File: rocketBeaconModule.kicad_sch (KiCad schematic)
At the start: 36 parts, among them J1 TYPE-C-31-M-12, J2 Jumper Select, J3 Main Bus, U1 STM32F401CCU6, U2 AMS1117-3.3, Y1 16MHz

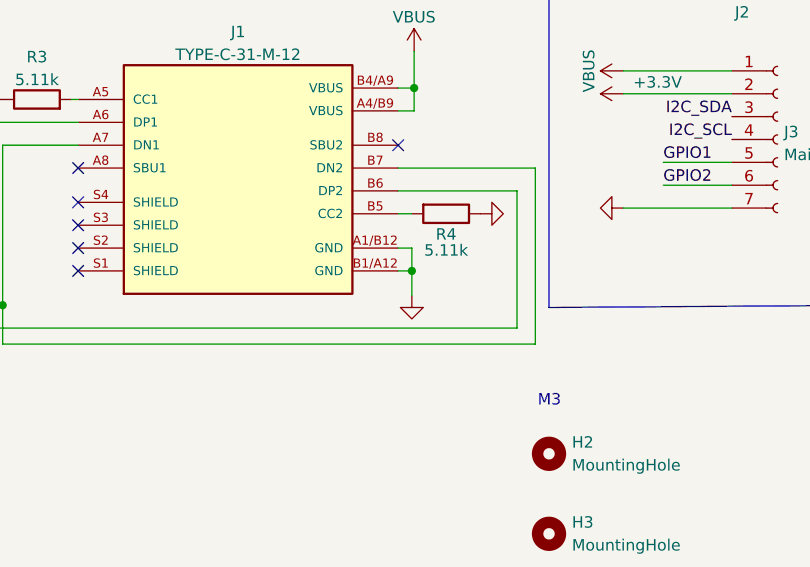
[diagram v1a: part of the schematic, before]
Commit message: removed old footprints and replaced with new ones
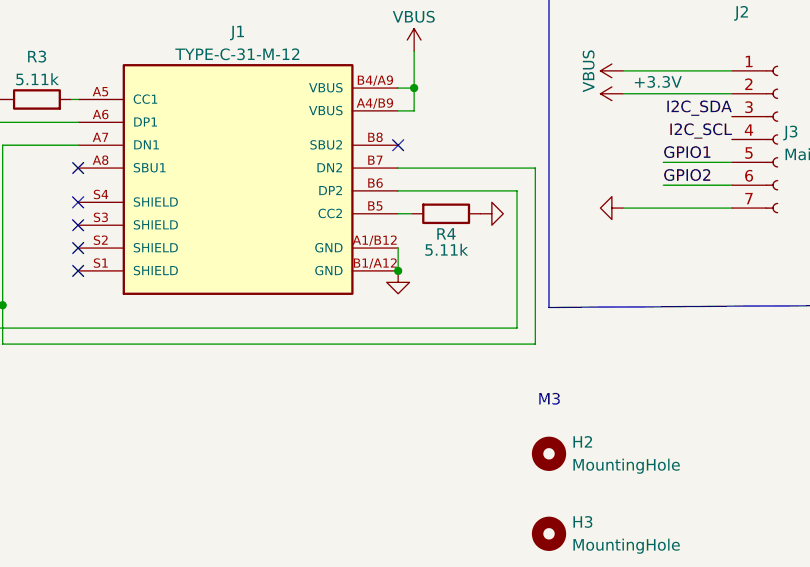
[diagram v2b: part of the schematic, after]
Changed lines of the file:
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@@
   (junction (at 88.9 24.13) (diameter 0) (color 0 0 0 0)
   )
-  (junction (at 233.68 102.87) (diameter 0) (color 0 0 0 0)
-  )
   (junction (at 135.89 124.46) (diameter 0) (color 0 0 0 0)
   )
@@
   )
   (junction (at 129.54 36.83) (diameter 0) (color 0 0 0 0)
+  )
+  (junction (at 232.156 102.87) (diameter 0) (color 0 0 0 0)
   )
   (junction (at 88.9 36.83) (diameter 0) (color 0 0 0 0)
@@
   (no_connect (at 118.11 76.2))
   (no_connect (at 118.11 101.6))
-  (wire (pts (xy 233.68 100.33) (xy 233.68 102.87))
-    (stroke (width 0) (type default) (color 0 0 0 0))
-  )
   (wire (pts (xy 135.89 121.92) (xy 135.89 124.46))
     (stroke (width 0) (type default) (color 0 0 0 0))
@@
     (stroke (width 0) (type default) (color 0 0 0 0))
   )
-  (wire (pts (xy 233.68 102.87) (xy 233.68 105.664))
-    (stroke (width 0) (type default) (color 0 0 0 0))
-  )
   (wire (pts (xy 247.396 110.998) (xy 188.214 110.998))
     (stroke (width 0) (type default) (color 0 0 0 0))
@@
     (stroke (width 0) (type default) (color 0 0 0 0))
   )
-  (wire (pts (xy 232.156 100.33) (xy 233.68 100.33))
-    (stroke (width 0) (type default) (color 0 0 0 0))
-  )
   (wire (pts (xy 137.16 36.83) (xy 134.62 36.83))
     (stroke (width 0) (type default) (color 0 0 0 0))
@@
     (stroke (width 0) (type default) (color 0 0 0 0))
   )
-  (wire (pts (xy 232.156 102.87) (xy 233.68 102.87))
-    (stroke (width 0) (type default) (color 0 0 0 0))
-  )
   (wire (pts (xy 88.9 74.93) (xy 88.9 82.55))
     (stroke (width 0) (type default) (color 0 0 0 0))
@@
   )
   (wire (pts (xy 237.49 39.37) (xy 224.79 39.37))
+    (stroke (width 0) (type default) (color 0 0 0 0))
+  )
+  (wire (pts (xy 232.156 100.33) (xy 232.156 102.87))
     (stroke (width 0) (type default) (color 0 0 0 0))
   )
@@
     (pin "1")
     (pin "2")
-  )
-  (symbol (lib_id "power:GND") (at 233.68 105.664 0) (unit 1)
-    (in_bom yes) (on_board yes) (fields_autoplaced)
-    (property "Reference" "#PWR?" (id 0) (at 233.68 112.014 0)
-      (effects (font (size 1.27 1.27)) hide)
-    )
-    (property "Value" "GND" (id 1) (at 233.68 110.744 0)
-      (effects (font (size 1.27 1.27)) hide)
-    )
-    (property "Footprint" "" (id 2) (at 233.68 105.664 0)
-      (effects (font (size 1.27 1.27)) hide)
-    )
-    (property "Datasheet" "" (id 3) (at 233.68 105.664 0)
-      (effects (font (size 1.27 1.27)) hide)
-    )
-    (pin "1")
   )
   (symbol (lib_id "Device:C") (at 114.3 30.48 0) (unit 1)
@@
     (pin "1")
     (pin "2")
+  )
+  (symbol (lib_id "power:GND") (at 232.156 102.87 0) (unit 1)
+    (in_bom yes) (on_board yes) (fields_autoplaced)
+    (property "Reference" "#PWR?" (id 0) (at 232.156 109.22 0)
+      (effects (font (size 1.27 1.27)) hide)
+    )
+    (property "Value" "GND" (id 1) (at 232.156 107.95 0)
+      (effects (font (size 1.27 1.27)) hide)
+    )
+    (property "Footprint" "" (id 2) (at 232.156 102.87 0)
+      (effects (font (size 1.27 1.27)) hide)
+    )
+    (property "Datasheet" "" (id 3) (at 232.156 102.87 0)
+      (effects (font (size 1.27 1.27)) hide)
+    )
+    (pin "1")
   )
   (symbol (lib_id "Device:C") (at 72.39 86.36 0) (unit 1)
@@
       (reference "#PWR052") (unit 1) (value "GND") (footprint "")
     )
-    (path "/2524f07a-7700-4c73-8c46-760211bff96a"
+    (path "/d5f8a67e-49ef-4272-8911-e8297d81e01b"
       (reference "#PWR?") (unit 1) (value "GND") (footprint "")
     )
